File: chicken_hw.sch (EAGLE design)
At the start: 3 parts

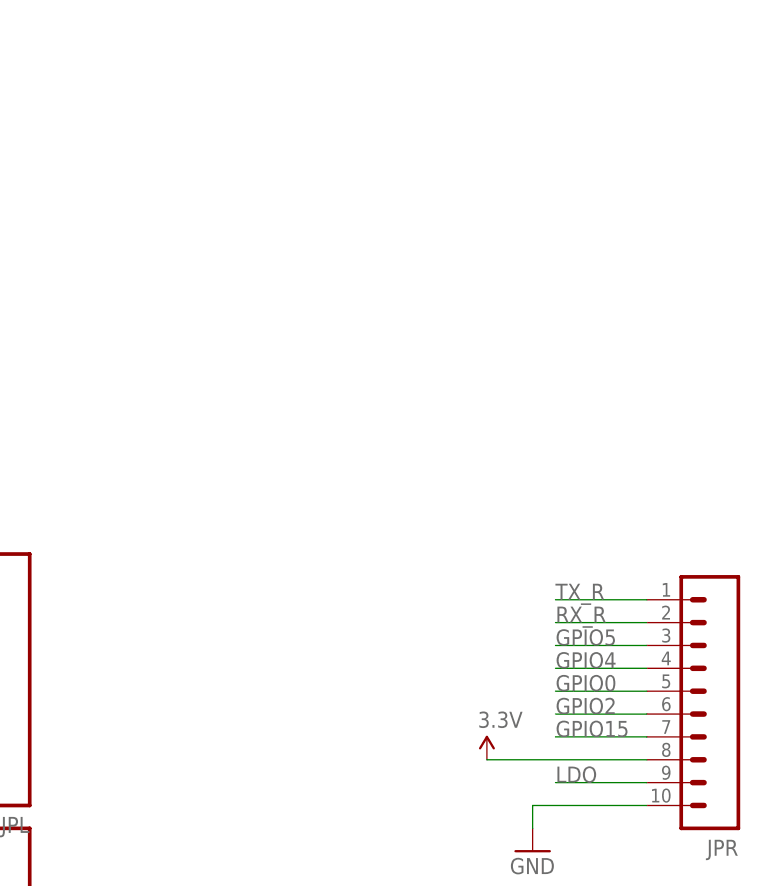
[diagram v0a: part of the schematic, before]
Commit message: Start adding analog mux to design
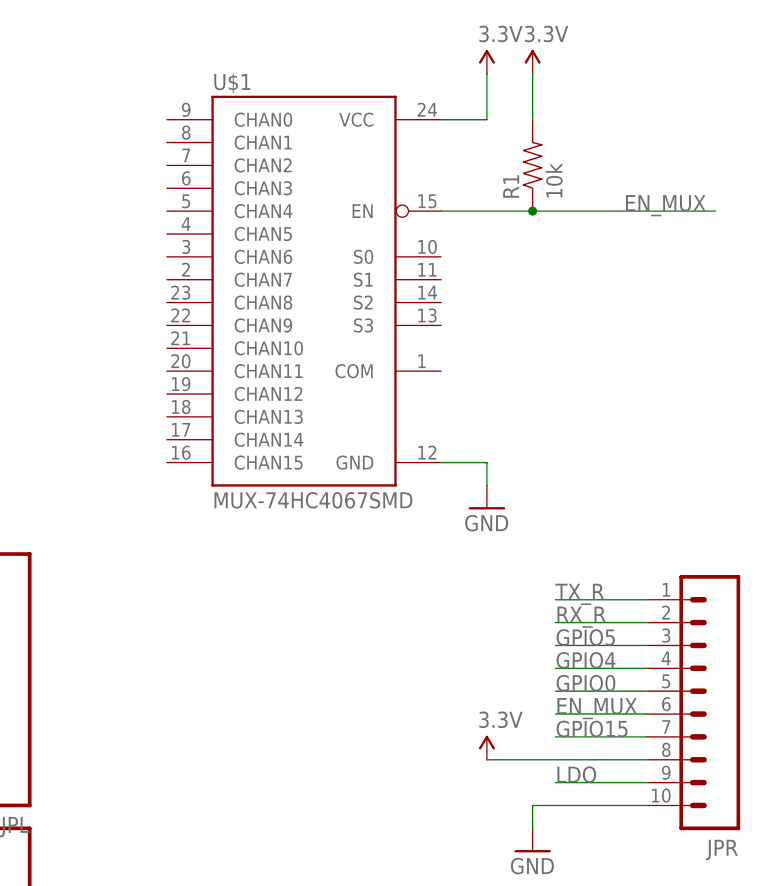
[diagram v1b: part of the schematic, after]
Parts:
- added R1: 10k, SparkFun-Resistors:RESISTORPTH-1/4W
- added U$1: MUX-74HC4067SMD, SparkFun-AnalogIC:MUX-74HC4067SMD
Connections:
- removed net GPIO2: JPR.6
- new net EN_MUX: JPR.6, R1.1, U$1.EN
- net 3.3V: now also R1.2, U$1.VCC
- net GND: now also U$1.GND
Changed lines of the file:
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@@
 <part name="GND3" library="SparkFun-Aesthetics" deviceset="GND" device=""/>
 <part name="SUPPLY1" library="SparkFun-Aesthetics" deviceset="3.3V" device=""/>
+<part name="U$1" library="SparkFun-AnalogIC" deviceset="MUX-74HC4067" device="SMD"/>
+<part name="SUPPLY2" library="SparkFun-Aesthetics" deviceset="3.3V" device=""/>
+<part name="GND4" library="SparkFun-Aesthetics" deviceset="GND" device=""/>
+<part name="R1" library="SparkFun-Resistors" deviceset="RESISTOR" device="PTH-1/4W" value="10k"/>
+<part name="SUPPLY3" library="SparkFun-Aesthetics" deviceset="3.3V" device=""/>
 </parts>
 <sheets>
@@
 <instance part="GND3" gate="1" x="-15.24" y="17.78"/>
 <instance part="SUPPLY1" gate="G$1" x="60.96" y="25.4"/>
+<instance part="U$1" gate="G$1" x="40.64" y="78.74"/>
+<instance part="SUPPLY2" gate="G$1" x="60.96" y="101.6"/>
+<instance part="GND4" gate="1" x="60.96" y="53.34"/>
+<instance part="R1" gate="G$1" x="66.04" y="91.44" rot="R90"/>
+<instance part="SUPPLY3" gate="G$1" x="66.04" y="101.6"/>
 </instances>
 <busses>
@@
 </segment>
 </net>
-<net name="GPIO2" class="0">
-<segment>
-<pinref part="JPR" gate="G$1" pin="6"/>
-<wire x1="78.74" y1="30.48" x2="68.58" y2="30.48" width="0.1524" layer="91"/>
-<label x="68.58" y="30.48" size="1.778" layer="95"/>
-</segment>
-</net>
 <net name="GPIO0" class="0">
 <segment>
@@
 <wire x1="0" y1="22.86" x2="-15.24" y2="22.86" width="0.1524" layer="91"/>
 </segment>
+<segment>
+<pinref part="U$1" gate="G$1" pin="GND"/>
+<wire x1="55.88" y1="58.42" x2="60.96" y2="58.42" width="0.1524" layer="91"/>
+<pinref part="GND4" gate="1" pin="GND"/>
+<wire x1="60.96" y1="58.42" x2="60.96" y2="55.88" width="0.1524" layer="91"/>
+</segment>
 </net>
 <net name="N$11" class="0">
@@
 <pinref part="SUPPLY1" gate="G$1" pin="3.3V"/>
 </segment>
-</net>
+<segment>
+<pinref part="U$1" gate="G$1" pin="VCC"/>
+<wire x1="55.88" y1="96.52" x2="60.96" y2="96.52" width="0.1524" layer="91"/>
+<pinref part="SUPPLY2" gate="G$1" pin="3.3V"/>
+<wire x1="60.96" y1="96.52" x2="60.96" y2="101.6" width="0.1524" layer="91"/>
+</segment>
+<segment>
+<pinref part="R1" gate="G$1" pin="2"/>
+<pinref part="SUPPLY3" gate="G$1" pin="3.3V"/>
+<wire x1="66.04" y1="96.52" x2="66.04" y2="101.6" width="0.1524" layer="91"/>
+</segment>
+</net>
+<net name="EN_MUX" class="0">
+<segment>
+<pinref part="U$1" gate="G$1" pin="EN"/>
+<pinref part="R1" gate="G$1" pin="1"/>
+<wire x1="55.88" y1="86.36" x2="66.04" y2="86.36" width="0.1524" layer="91"/>
+<wire x1="66.04" y1="86.36" x2="86.36" y2="86.36" width="0.1524" layer="91"/>
+<junction x="66.04" y="86.36"/>
+<label x="76.2" y="86.36" size="1.778" layer="95"/>
+</segment>
+<segment>
+<pinref part="JPR" gate="G$1" pin="6"/>
+<wire x1="78.74" y1="30.48" x2="68.58" y2="30.48" width="0.1524" layer="91"/>
+<label x="68.58" y="30.48" size="1.778" layer="95"/>
+</segment>
+</net>

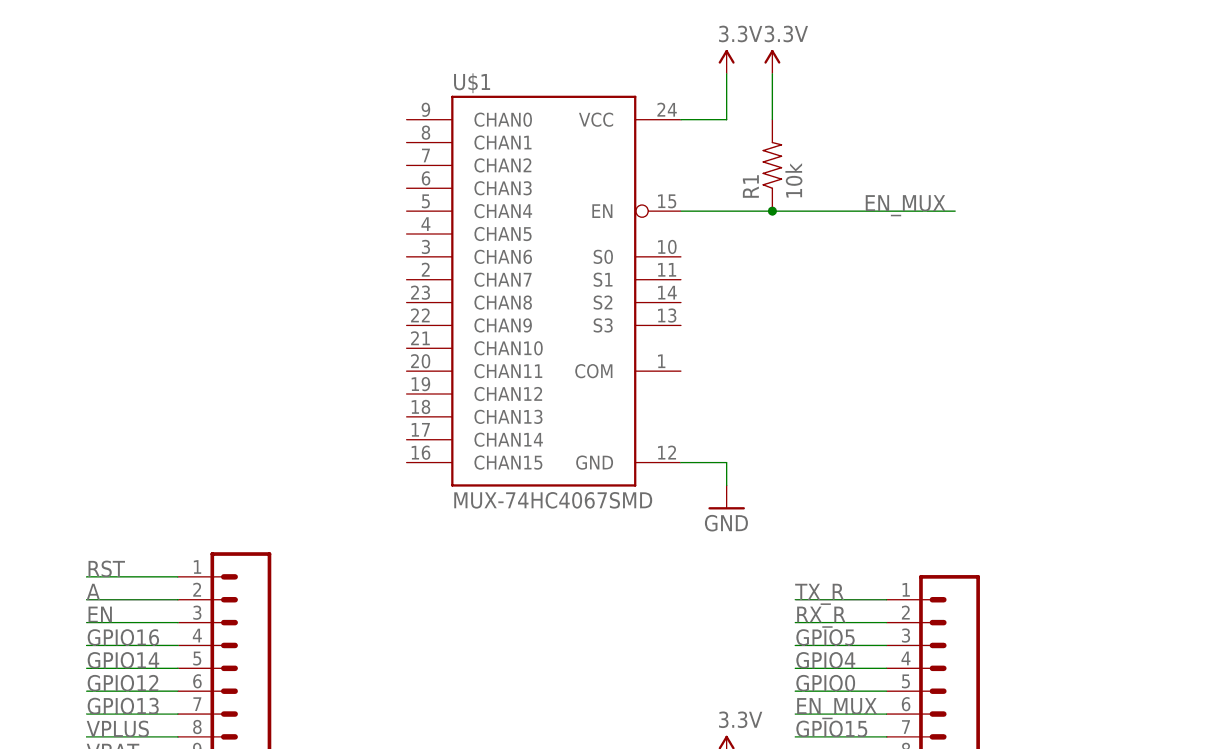
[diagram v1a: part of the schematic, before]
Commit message: Rough placement of components on board design
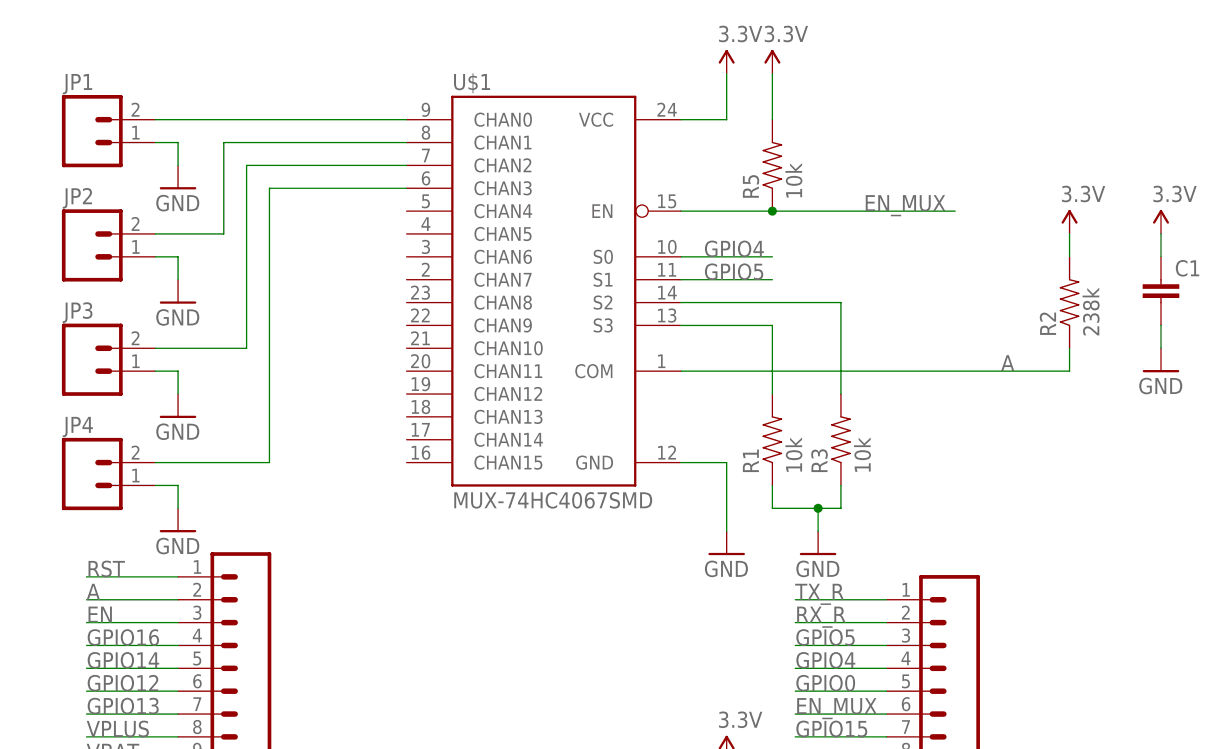
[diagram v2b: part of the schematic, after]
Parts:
- added C1: (no value), SparkFun-Capacitors:CAP0603-CAP
- added JP1, JP2, JP3, JP4: (no value), SparkFun-Connectors:M02PTH
- added R2: 238k, SparkFun-Resistors:RESISTOR0603
- added R3, R5: 10k, SparkFun-Resistors:RESISTOR0603
- R1: device SparkFun-Resistors:RESISTORPTH-1/4W -> SparkFun-Resistors:RESISTOR0603
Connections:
- new net N$1: R1.2, U$1.S3
- new net N$2: JP1.2, U$1.CHAN0
- new net N$3: JP2.2, U$1.CHAN1
- new net N$4: JP3.2, U$1.CHAN2
- new net N$5: JP4.2, U$1.CHAN3
- new net N$6: R3.2, U$1.S2
- net 3.3V: now also C1.1, R2.2, R5.2; no longer R1.2
- net A: now also R2.1, U$1.COM
- net EN_MUX: now also R5.1; no longer R1.1
- net GND: now also C1.2, JP1.1, JP2.1, JP3.1, JP4.1, R1.1, R3.1
- net GPIO4: now also U$1.S0
- net GPIO5: now also U$1.S1
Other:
- moved on the sheet: R1
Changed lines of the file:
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@@
 <layer number="112" name="tSilk" color="7" fill="1" visible="no" active="yes"/>
 <layer number="113" name="IDFDebug" color="4" fill="1" visible="no" active="yes"/>
+<layer number="114" name="Badge_Outline" color="7" fill="1" visible="yes" active="yes"/>
+<layer number="115" name="ReferenceISLANDS" color="7" fill="1" visible="yes" active="yes"/>
 <layer number="116" name="Patch_BOT" color="9" fill="4" visible="no" active="yes"/>
 <layer number="118" name="Rect_Pads" color="7" fill="1" visible="yes" active="yes"/>
@@
 <part name="SUPPLY2" library="SparkFun-Aesthetics" deviceset="3.3V" device=""/>
 <part name="GND4" library="SparkFun-Aesthetics" deviceset="GND" device=""/>
-<part name="R1" library="SparkFun-Resistors" deviceset="RESISTOR" device="PTH-1/4W" value="10k"/>
 <part name="SUPPLY3" library="SparkFun-Aesthetics" deviceset="3.3V" device=""/>
+<part name="SUPPLY4" library="SparkFun-Aesthetics" deviceset="3.3V" device=""/>
+<part name="JP1" library="SparkFun-Connectors" deviceset="M02" device="PTH"/>
+<part name="JP2" library="SparkFun-Connectors" deviceset="M02" device="PTH"/>
+<part name="JP3" library="SparkFun-Connectors" deviceset="M02" device="PTH"/>
+<part name="JP4" library="SparkFun-Connectors" deviceset="M02" device="PTH"/>
+<part name="GND5" library="SparkFun-Aesthetics" deviceset="GND" device=""/>
+<part name="GND6" library="SparkFun-Aesthetics" deviceset="GND" device=""/>
+<part name="GND7" library="SparkFun-Aesthetics" deviceset="GND" device=""/>
+<part name="GND8" library="SparkFun-Aesthetics" deviceset="GND" device=""/>
+<part name="GND9" library="SparkFun-Aesthetics" deviceset="GND" device=""/>
+<part name="SUPPLY5" library="SparkFun-Aesthetics" deviceset="3.3V" device=""/>
+<part name="GND10" library="SparkFun-Aesthetics" deviceset="GND" device=""/>
+<part name="C1" library="SparkFun-Capacitors" deviceset="CAP" device="0603-CAP"/>
+<part name="R5" library="SparkFun-Resistors" deviceset="RESISTOR" device="0603" value="10k"/>
+<part name="R1" library="SparkFun-Resistors" deviceset="RESISTOR" device="0603" value="10k"/>
+<part name="R3" library="SparkFun-Resistors" deviceset="RESISTOR" device="0603" value="10k"/>
+<part name="R2" library="SparkFun-Resistors" deviceset="RESISTOR" device="0603" value="238k"/>
 </parts>
 <sheets>
@@
 <instance part="U$1" gate="G$1" x="40.64" y="78.74"/>
 <instance part="SUPPLY2" gate="G$1" x="60.96" y="101.6"/>
-<instance part="GND4" gate="1" x="60.96" y="53.34"/>
-<instance part="R1" gate="G$1" x="66.04" y="91.44" rot="R90"/>
+<instance part="GND4" gate="1" x="60.96" y="48.26"/>
 <instance part="SUPPLY3" gate="G$1" x="66.04" y="101.6"/>
+<instance part="SUPPLY4" gate="G$1" x="99.06" y="83.82"/>
+<instance part="JP1" gate="G$1" x="-10.16" y="93.98"/>
+<instance part="JP2" gate="G$1" x="-10.16" y="81.28"/>
+<instance part="JP3" gate="G$1" x="-10.16" y="68.58"/>
+<instance part="JP4" gate="G$1" x="-10.16" y="55.88"/>
+<instance part="GND5" gate="1" x="0" y="50.8"/>
+<instance part="GND6" gate="1" x="0" y="63.5"/>
+<instance part="GND7" gate="1" x="0" y="76.2"/>
+<instance part="GND8" gate="1" x="0" y="88.9"/>
+<instance part="GND9" gate="1" x="71.12" y="48.26"/>
+<instance part="SUPPLY5" gate="G$1" x="109.22" y="83.82"/>
+<instance part="GND10" gate="1" x="109.22" y="68.58"/>
+<instance part="C1" gate="G$1" x="109.22" y="76.2"/>
+<instance part="R5" gate="G$1" x="66.04" y="91.44" rot="R90"/>
+<instance part="R1" gate="G$1" x="66.04" y="60.96" rot="R90"/>
+<instance part="R3" gate="G$1" x="73.66" y="60.96" rot="R90"/>
+<instance part="R2" gate="G$1" x="99.06" y="76.2" rot="R90"/>
 </instances>
 <busses>
@@
 <label x="-10.16" y="43.18" size="1.778" layer="95"/>
 </segment>
+<segment>
+<pinref part="U$1" gate="G$1" pin="COM"/>
+<wire x1="55.88" y1="68.58" x2="99.06" y2="68.58" width="0.1524" layer="91"/>
+<label x="91.44" y="68.58" size="1.778" layer="95"/>
+<wire x1="99.06" y1="68.58" x2="99.06" y2="71.12" width="0.1524" layer="91"/>
+<pinref part="R2" gate="G$1" pin="1"/>
+</segment>
 </net>
 <net name="EN" class="0">
@@
 <label x="68.58" y="35.56" size="1.778" layer="95"/>
 </segment>
+<segment>
+<pinref part="U$1" gate="G$1" pin="S0"/>
+<wire x1="55.88" y1="81.28" x2="66.04" y2="81.28" width="0.1524" layer="91"/>
+<label x="58.42" y="81.28" size="1.778" layer="95"/>
+</segment>
 </net>
 <net name="GPIO5" class="0">
@@
 <wire x1="78.74" y1="38.1" x2="68.58" y2="38.1" width="0.1524" layer="91"/>
 <label x="68.58" y="38.1" size="1.778" layer="95"/>
+</segment>
+<segment>
+<pinref part="U$1" gate="G$1" pin="S1"/>
+<wire x1="55.88" y1="78.74" x2="66.04" y2="78.74" width="0.1524" layer="91"/>
+<label x="58.42" y="78.74" size="1.778" layer="95"/>
 </segment>
 </net>
@@
 <wire x1="55.88" y1="58.42" x2="60.96" y2="58.42" width="0.1524" layer="91"/>
 <pinref part="GND4" gate="1" pin="GND"/>
-<wire x1="60.96" y1="58.42" x2="60.96" y2="55.88" width="0.1524" layer="91"/>
+<wire x1="60.96" y1="58.42" x2="60.96" y2="50.8" width="0.1524" layer="91"/>
+</segment>
+<segment>
+<pinref part="JP1" gate="G$1" pin="1"/>
+<wire x1="-2.54" y1="93.98" x2="0" y2="93.98" width="0.1524" layer="91"/>
+<pinref part="GND8" gate="1" pin="GND"/>
+<wire x1="0" y1="93.98" x2="0" y2="91.44" width="0.1524" layer="91"/>
+</segment>
+<segment>
+<pinref part="GND7" gate="1" pin="GND"/>
+<wire x1="0" y1="78.74" x2="0" y2="81.28" width="0.1524" layer="91"/>
+<pinref part="JP2" gate="G$1" pin="1"/>
+<wire x1="0" y1="81.28" x2="-2.54" y2="81.28" width="0.1524" layer="91"/>
+</segment>
+<segment>
+<pinref part="GND6" gate="1" pin="GND"/>
+<wire x1="0" y1="66.04" x2="0" y2="68.58" width="0.1524" layer="91"/>
+<pinref part="JP3" gate="G$1" pin="1"/>
+<wire x1="0" y1="68.58" x2="-2.54" y2="68.58" width="0.1524" layer="91"/>
+</segment>
+<segment>
+<pinref part="GND5" gate="1" pin="GND"/>
+<wire x1="0" y1="53.34" x2="0" y2="55.88" width="0.1524" layer="91"/>
+<pinref part="JP4" gate="G$1" pin="1"/>
+<wire x1="0" y1="55.88" x2="-2.54" y2="55.88" width="0.1524" layer="91"/>
+</segment>
+<segment>
+<wire x1="66.04" y1="55.88" x2="66.04" y2="53.34" width="0.1524" layer="91"/>
+<wire x1="66.04" y1="53.34" x2="71.12" y2="53.34" width="0.1524" layer="91"/>
+<pinref part="GND9" gate="1" pin="GND"/>
+<wire x1="71.12" y1="53.34" x2="73.66" y2="53.34" width="0.1524" layer="91"/>
+<wire x1="73.66" y1="53.34" x2="73.66" y2="55.88" width="0.1524" layer="91"/>
+<wire x1="71.12" y1="50.8" x2="71.12" y2="53.34" width="0.1524" layer="91"/>
+<junction x="71.12" y="53.34"/>
+<pinref part="R1" gate="G$1" pin="1"/>
+<pinref part="R3" gate="G$1" pin="1"/>
+</segment>
+<segment>
+<pinref part="GND10" gate="1" pin="GND"/>
+<pinref part="C1" gate="G$1" pin="2"/>
+<wire x1="109.22" y1="71.12" x2="109.22" y2="73.66" width="0.1524" layer="91"/>
 </segment>
 </net>
@@
 </segment>
 <segment>
-<pinref part="R1" gate="G$1" pin="2"/>
 <pinref part="SUPPLY3" gate="G$1" pin="3.3V"/>
 <wire x1="66.04" y1="96.52" x2="66.04" y2="101.6" width="0.1524" layer="91"/>
+<pinref part="R5" gate="G$1" pin="2"/>
+</segment>
+<segment>
+<pinref part="SUPPLY4" gate="G$1" pin="3.3V"/>
+<wire x1="99.06" y1="83.82" x2="99.06" y2="81.28" width="0.1524" layer="91"/>
+<pinref part="R2" gate="G$1" pin="2"/>
+</segment>
+<segment>
+<pinref part="C1" gate="G$1" pin="1"/>
+<pinref part="SUPPLY5" gate="G$1" pin="3.3V"/>
+<wire x1="109.22" y1="81.28" x2="109.22" y2="83.82" width="0.1524" layer="91"/>
 </segment>
 </net>
@@
 <segment>
 <pinref part="U$1" gate="G$1" pin="EN"/>
-<pinref part="R1" gate="G$1" pin="1"/>
 <wire x1="55.88" y1="86.36" x2="66.04" y2="86.36" width="0.1524" layer="91"/>
+<label x="76.2" y="86.36" size="1.778" layer="95"/>
+<pinref part="R5" gate="G$1" pin="1"/>
 <wire x1="66.04" y1="86.36" x2="86.36" y2="86.36" width="0.1524" layer="91"/>
 <junction x="66.04" y="86.36"/>
-<label x="76.2" y="86.36" size="1.778" layer="95"/>
 </segment>
 <segment>
@@
 </segment>
 </net>
+<net name="N$2" class="0">
+<segment>
+<pinref part="JP1" gate="G$1" pin="2"/>
+<pinref part="U$1" gate="G$1" pin="CHAN0"/>
+<wire x1="-2.54" y1="96.52" x2="25.4" y2="96.52" width="0.1524" layer="91"/>
+</segment>
+</net>
+<net name="N$3" class="0">
+<segment>
+<pinref part="JP2" gate="G$1" pin="2"/>
+<wire x1="-2.54" y1="83.82" x2="5.08" y2="83.82" width="0.1524" layer="91"/>
+<wire x1="5.08" y1="83.82" x2="5.08" y2="93.98" width="0.1524" layer="91"/>
+<pinref part="U$1" gate="G$1" pin="CHAN1"/>
+<wire x1="5.08" y1="93.98" x2="25.4" y2="93.98" width="0.1524" layer="91"/>
+</segment>
+</net>
+<net name="N$4" class="0">
+<segment>
+<pinref part="JP3" gate="G$1" pin="2"/>
+<wire x1="-2.54" y1="71.12" x2="7.62" y2="71.12" width="0.1524" layer="91"/>
+<wire x1="7.62" y1="71.12" x2="7.62" y2="91.44" width="0.1524" layer="91"/>
+<pinref part="U$1" gate="G$1" pin="CHAN2"/>
+<wire x1="7.62" y1="91.44" x2="25.4" y2="91.44" width="0.1524" layer="91"/>
+</segment>
+</net>
+<net name="N$5" class="0">
+<segment>
+<pinref part="JP4" gate="G$1" pin="2"/>
+<wire x1="-2.54" y1="58.42" x2="10.16" y2="58.42" width="0.1524" layer="91"/>
+<wire x1="10.16" y1="58.42" x2="10.16" y2="88.9" width="0.1524" layer="91"/>
+<pinref part="U$1" gate="G$1" pin="CHAN3"/>
+<wire x1="10.16" y1="88.9" x2="25.4" y2="88.9" width="0.1524" layer="91"/>
+</segment>
+</net>
+<net name="N$1" class="0">
+<segment>
+<pinref part="U$1" gate="G$1" pin="S3"/>
+<wire x1="55.88" y1="73.66" x2="66.04" y2="73.66" width="0.1524" layer="91"/>
+<wire x1="66.04" y1="73.66" x2="66.04" y2="66.04" width="0.1524" layer="91"/>
+<pinref part="R1" gate="G$1" pin="2"/>
+</segment>
+</net>
+<net name="N$6" class="0">
+<segment>
+<pinref part="U$1" gate="G$1" pin="S2"/>
+<wire x1="55.88" y1="76.2" x2="73.66" y2="76.2" width="0.1524" layer="91"/>
+<wire x1="73.66" y1="76.2" x2="73.66" y2="66.04" width="0.1524" layer="91"/>
+<pinref part="R3" gate="G$1" pin="2"/>
+</segment>
+</net>

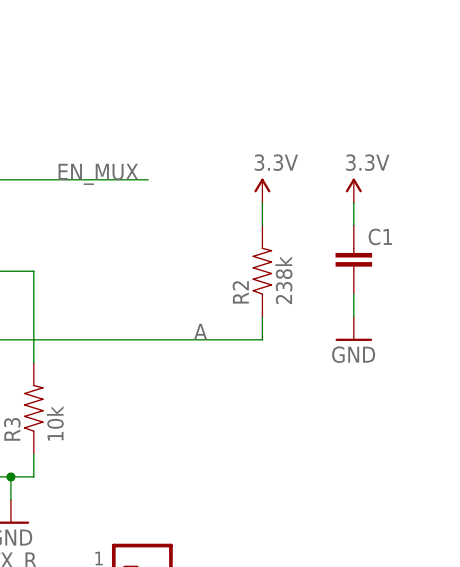
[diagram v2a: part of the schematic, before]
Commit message: Final initial placement of components, ready for autorouting
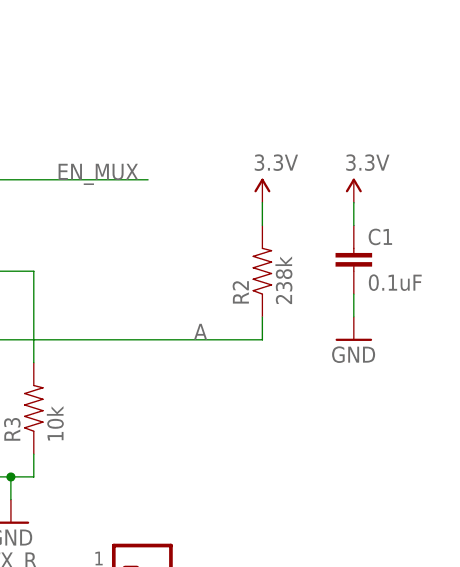
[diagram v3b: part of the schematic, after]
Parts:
- C1: value (none) -> 0.1uF
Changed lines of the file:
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@@
 <part name="SUPPLY5" library="SparkFun-Aesthetics" deviceset="3.3V" device=""/>
 <part name="GND10" library="SparkFun-Aesthetics" deviceset="GND" device=""/>
-<part name="C1" library="SparkFun-Capacitors" deviceset="CAP" device="0603-CAP"/>
+<part name="C1" library="SparkFun-Capacitors" deviceset="CAP" device="0603-CAP" value="0.1uF"/>
 <part name="R5" library="SparkFun-Resistors" deviceset="RESISTOR" device="0603" value="10k"/>
 <part name="R1" library="SparkFun-Resistors" deviceset="RESISTOR" device="0603" value="10k"/>
